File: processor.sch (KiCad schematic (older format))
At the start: 17 parts, among them U100 MC68000, U103 74F245, U104 74LS373, U105 74F245, U106 74LS373, U303 74F08

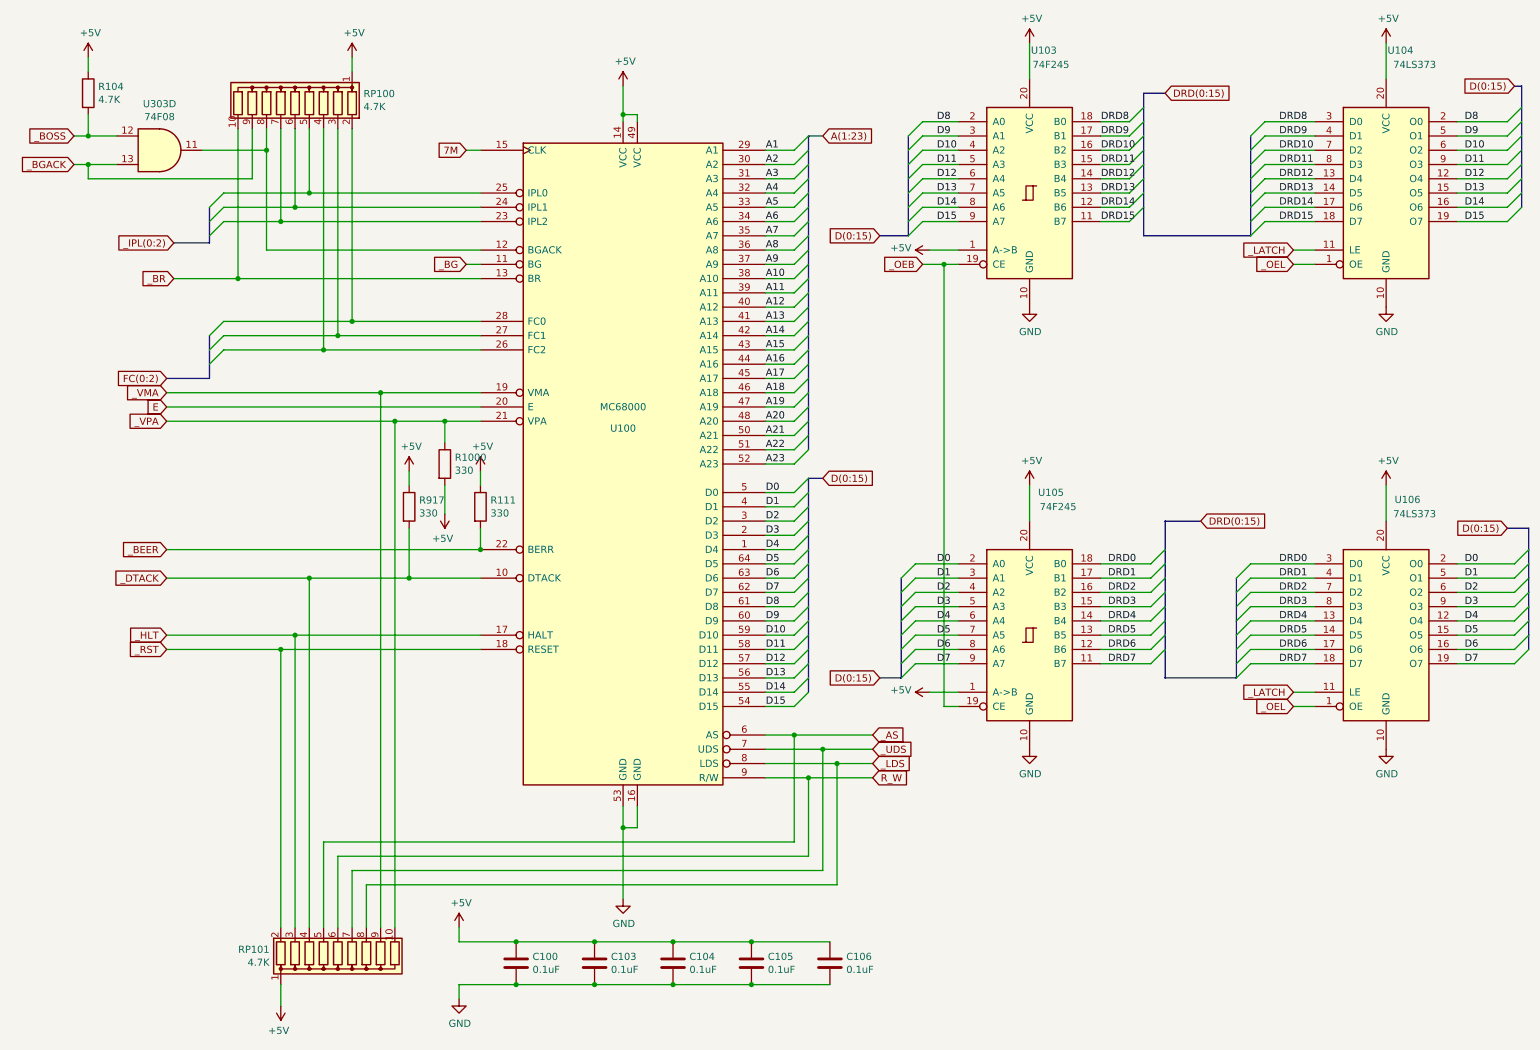
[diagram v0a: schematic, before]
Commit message: Rename bus with correct syntax
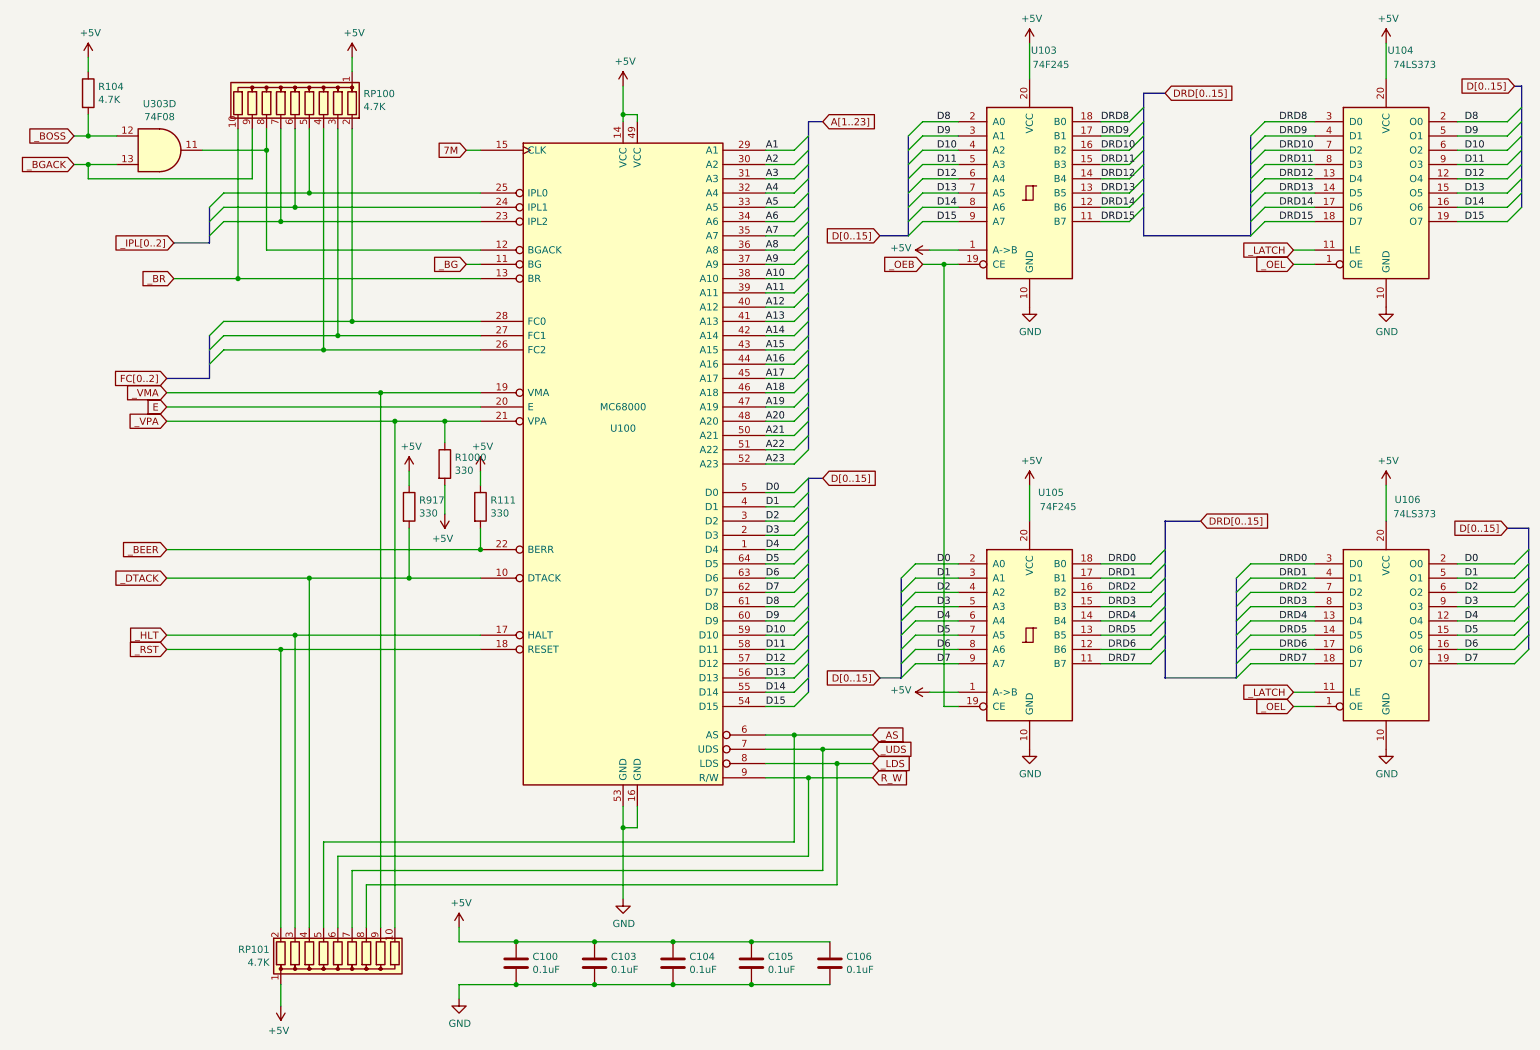
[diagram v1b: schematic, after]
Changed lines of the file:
@@
-EESchema Schematic File Version 4
+EESchema Schematic File Version 5
 LIBS:amiga2000-cache
 EELAYER 29 0
@@
 Wire Bus Line
 	6050 3850 6150 3850
-Wire Bus Line
-	6050 1450 6150 1450
-Text GLabel 6150 1450 2    50   Input ~ 0
-A(1:23)
+Text GLabel 6150 1350 2    50   Input ~ 0
+A[1..23]
 Text GLabel 6150 3850 2    50   Input ~ 0
-D(0:15)
+D[0..15]
 Wire Wire Line
 	3750 4350 1550 4350
@@
 	1850 2200 1600 2200
 Text GLabel 1600 2200 0    50   Input ~ 0
-_IPL(0:2)
+_IPL[0..2]
 Wire Wire Line
 	3750 2250 2250 2250
@@
 	1850 3050 1950 2950
 Text GLabel 1550 3150 0    50   Input ~ 0
-FC(0:2)
+FC[0..2]
 Wire Bus Line
 	1550 3150 1850 3150
@@
 	6550 5250 6700 5250
 Text GLabel 6550 2150 0    50   Input ~ 0
-D(0:15)
+D[0..15]
 Text GLabel 6550 5250 0    50   Input ~ 0
-D(0:15)
+D[0..15]
 Text GLabel 9450 2350 0    50   Input ~ 0
 _OEL
@@
 	8300 2050 8400 1950
 Text GLabel 8550 1150 2    50   Input ~ 0
-DRD(0:15)
+DRD[0..15]
 Text Label 8100 1350 0    50   ~ 0
 DRD8
@@
 	8450 5150 8550 5050
 Text GLabel 8800 4150 2    50   Input ~ 0
-DRD(0:15)
+DRD[0..15]
 Text Label 8150 4450 0    50   ~ 0
 DRD0
@@
 	8550 4150 8800 4150
 Text GLabel 11000 1100 0    50   Input ~ 0
-D(0:15)
+D[0..15]
 Text GLabel 10950 4200 0    50   Input ~ 0
-D(0:15)
+D[0..15]
 Text Label 10650 1350 0    50   ~ 0
 D8
@@
 	3500 3450 3150 3450
 Connection ~ 3750 4350
+Wire Bus Line
+	6050 1350 6150 1350
 $Comp
 L CPU_NXP_68000:68000D U100
@@
 	6050 3850 6050 5350
 Wire Bus Line
-	6050 1450 6050 3650
+	6050 1350 6050 3650
 $EndSCHEMATC

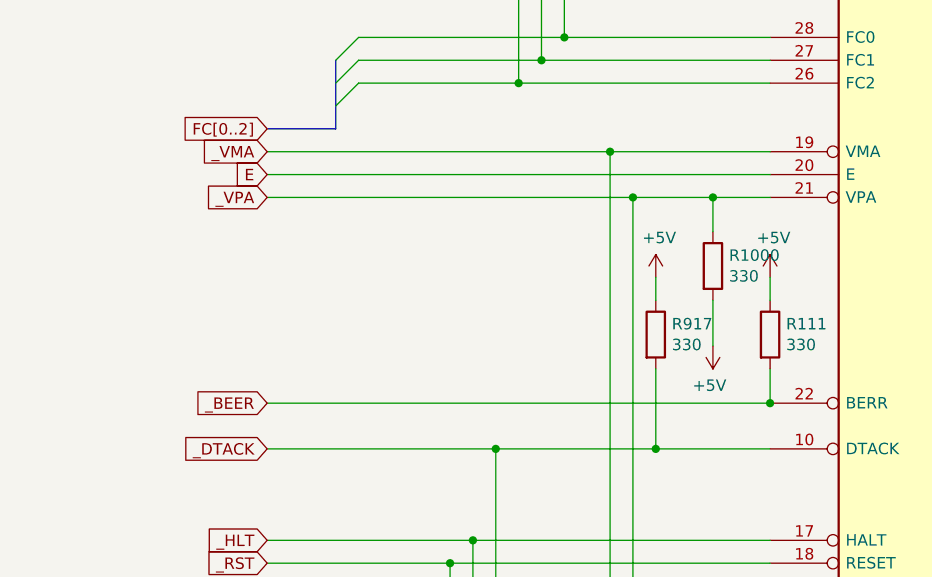
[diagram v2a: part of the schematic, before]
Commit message: Implemented various rev 6.2 fixes from forums and my own board
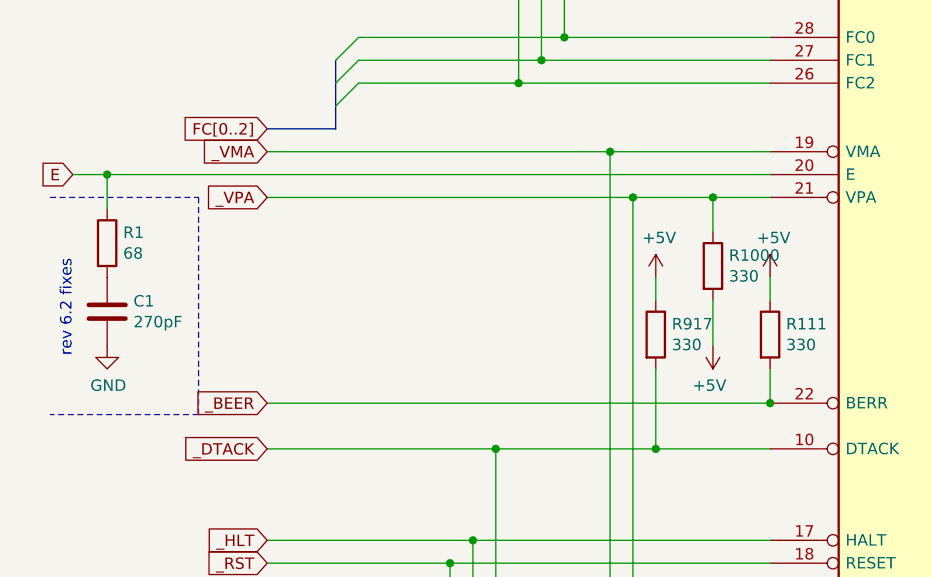
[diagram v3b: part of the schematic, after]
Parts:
- added C1: 270pF, symbol Device:C
- added R1: 68, symbol Device:R
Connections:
- net E: now also R1.1
- net GND: now also C1.2
- new net: C1.1, R1.2
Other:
- note added: "rev 6.2 fixes"
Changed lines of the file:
@@
 	3650 1550 3750 1550
 Wire Wire Line
-	1550 3350 3750 3350
-Text GLabel 1550 3350 0    50   Input ~ 0
+	700  3350 850  3350
+Text GLabel 700  3350 0    50   Input ~ 0
 E
 Wire Wire Line
@@
 	1    0    0    -1
 $EndComp
+$Comp
+L Device:R R1
+U 1 1 5D139FBE
+P 850 3650
+F 0 "R1" H 920 3696 50  0000 L CNN
+F 1 "68" H 920 3605 50  0000 L CNN
+F 2 "" V 780 3650 50  0001 C CNN
+F 3 "~" H 850 3650 50  0001 C CNN
+	1    850  3650
+	1    0    0    -1
+$EndComp
+$Comp
+L Device:C C1
+U 1 1 5D13AB75
+P 850 3950
+F 0 "C1" H 965 3996 50  0000 L CNN
+F 1 "270pF" H 965 3905 50  0000 L CNN
+F 2 "" H 888 3800 50  0001 C CNN
+F 3 "~" H 850 3950 50  0001 C CNN
+	1    850  3950
+	1    0    0    -1
+$EndComp
+$Comp
+L power:GND #PWR0262
+U 1 1 5D13B4A3
+P 850 4100
+F 0 "#PWR0262" H 850 3850 50  0001 C CNN
+F 1 "GND" H 855 3927 50  0000 C CNN
+F 2 "" H 850 4100 50  0001 C CNN
+F 3 "" H 850 4100 50  0001 C CNN
+	1    850  4100
+	1    0    0    -1
+$EndComp
+Wire Wire Line
+	850  3350 850  3500
+Connection ~ 850  3350
+Wire Wire Line
+	850  3350 3750 3350
+Wire Notes Line
+	600  3450 1250 3450
+Wire Notes Line
+	1250 3450 1250 4400
+Wire Notes Line
+	1250 4400 600  4400
 Wire Bus Line
 	1850 1950 1850 2200
@@
 Wire Bus Line
 	6050 1350 6050 3650
+Text Notes 700  4150 1    50   ~ 0
+rev 6.2 fixes
 $EndSCHEMATC

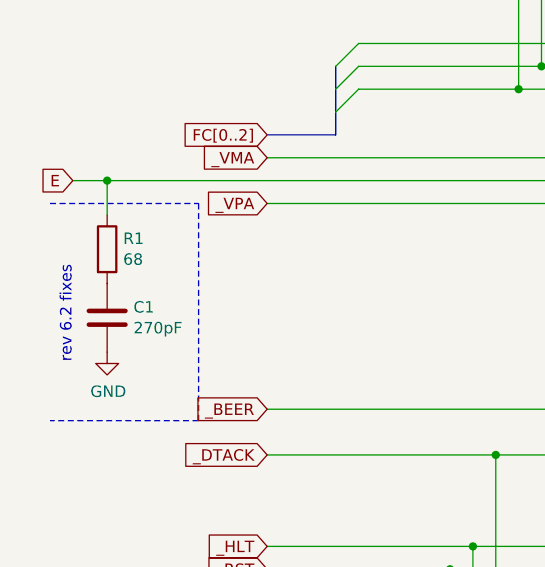
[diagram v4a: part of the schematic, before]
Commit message: Misread the PCB; It's effectively E and not A1
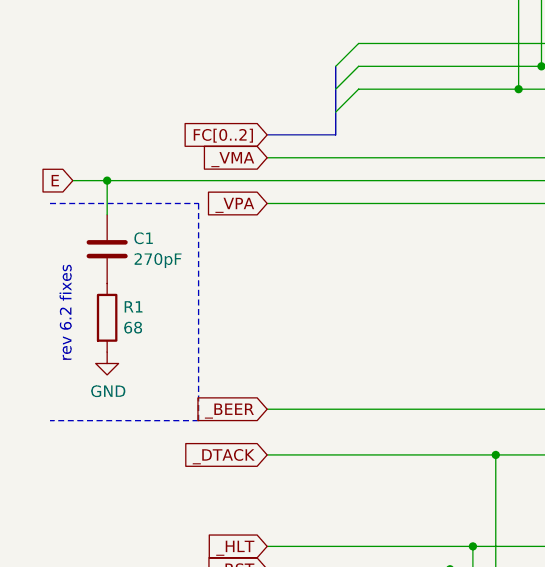
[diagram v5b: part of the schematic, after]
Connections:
- net E: now also C1.1; no longer R1.1
- net GND: now also R1.2; no longer C1.2
- new net: C1.2, R1.1
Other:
- moved on the sheet: C1, R1
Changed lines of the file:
@@
 L Device:R R1
 U 1 1 5D139FBE
-P 850 3650
-F 0 "R1" H 920 3696 50  0000 L CNN
-F 1 "68" H 920 3605 50  0000 L CNN
-F 2 "" V 780 3650 50  0001 C CNN
-F 3 "~" H 850 3650 50  0001 C CNN
-	1    850  3650
+P 850 3950
+F 0 "R1" H 920 3996 50  0000 L CNN
+F 1 "68" H 920 3905 50  0000 L CNN
+F 2 "" V 780 3950 50  0001 C CNN
+F 3 "~" H 850 3950 50  0001 C CNN
+	1    850  3950
 	1    0    0    -1
 $EndComp
@@
 L Device:C C1
 U 1 1 5D13AB75
-P 850 3950
-F 0 "C1" H 965 3996 50  0000 L CNN
-F 1 "270pF" H 965 3905 50  0000 L CNN
-F 2 "" H 888 3800 50  0001 C CNN
-F 3 "~" H 850 3950 50  0001 C CNN
-	1    850  3950
+P 850 3650
+F 0 "C1" H 965 3696 50  0000 L CNN
+F 1 "270pF" H 965 3605 50  0000 L CNN
+F 2 "" H 888 3500 50  0001 C CNN
+F 3 "~" H 850 3650 50  0001 C CNN
+	1    850  3650
 	1    0    0    -1
 $EndComp
@@
 Wire Notes Line
 	1250 4400 600  4400
+Text Notes 700  4150 1    50   ~ 0
+rev 6.2 fixes
 Wire Bus Line
 	1850 1950 1850 2200
@@
 Wire Bus Line
 	6050 1350 6050 3650
-Text Notes 700  4150 1    50   ~ 0
-rev 6.2 fixes
 $EndSCHEMATC

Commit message: Review started; oopsie whoopsie
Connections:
- net _IPL2: now reaches RP100.7 (R6), U100.23 (IPL2)
- net _IPL1: now reaches RP100.6 (R5), U100.24 (IPL1)
- net _IPL0: now reaches RP100.5 (R4), U100.25 (IPL0)
- net FC2: now reaches RP100.4 (R3), U100.26 (FC2)
- net FC1: now reaches RP100.3 (R2), U100.27 (FC1)
- net FC0: now reaches RP100.2 (R1), U100.28 (FC0)
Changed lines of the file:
@@
 Wire Bus Line
 	6050 1350 6050 3650
+Text Label 3500 1850 0    50   ~ 0
+_IPL0
+Text Label 3500 1950 0    50   ~ 0
+_IPL1
+Text Label 3500 2050 0    50   ~ 0
+_IPL2
+Text Label 3550 2750 0    50   ~ 0
+FC0
+Text Label 3550 2850 0    50   ~ 0
+FC1
+Text Label 3550 2950 0    50   ~ 0
+FC2
 $EndSCHEMATC

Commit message: Associate footprints with components
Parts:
- R1, R1000, R104, R111, R917: footprint (none) -> Resistor_THT:R_Axial_DIN0207_L6.3mm_D2.5mm_P10.16mm_Horizontal
- U103, U104, U105, U106: footprint (none) -> Package_DIP:DIP-20_W7.62mm_Socket
- U303: footprint (none) -> Package_DIP:DIP-14_W7.62mm_Socket
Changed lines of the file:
@@
 F 0 "U103" H 7700 2850 50  0000 C CNN
 F 1 "74F245" H 7750 2750 50  0000 C CNN
-F 2 "" H 7600 1850 50  0001 C CNN
+F 2 "Package_DIP:DIP-20_W7.62mm_Socket" H 7600 1850 50  0001 C CNN
 F 3 "http://www.ti.com/lit/gpn/sn74LS245" H 7600 1850 50  0001 C CNN
 	1    7600 1850
@@
 F 0 "U105" H 7750 5950 50  0000 C CNN
 F 1 "74F245" H 7800 5850 50  0000 C CNN
-F 2 "" H 7600 4950 50  0001 C CNN
+F 2 "Package_DIP:DIP-20_W7.62mm_Socket" H 7600 4950 50  0001 C CNN
 F 3 "http://www.ti.com/lit/gpn/sn74LS245" H 7600 4950 50  0001 C CNN
 	1    7600 4950
@@
 F 0 "U104" H 10200 2850 50  0000 C CNN
 F 1 "74LS373" H 10300 2750 50  0000 C CNN
-F 2 "" H 10100 1850 50  0001 C CNN
+F 2 "Package_DIP:DIP-20_W7.62mm_Socket" H 10100 1850 50  0001 C CNN
 F 3 "http://www.ti.com/lit/gpn/sn74LS373" H 10100 1850 50  0001 C CNN
 	1    10100 1850
@@
 F 0 "U106" H 10250 5900 50  0000 C CNN
 F 1 "74LS373" H 10300 5800 50  0000 C CNN
-F 2 "" H 10100 4950 50  0001 C CNN
+F 2 "Package_DIP:DIP-20_W7.62mm_Socket" H 10100 4950 50  0001 C CNN
 F 3 "http://www.ti.com/lit/gpn/sn74LS373" H 10100 4950 50  0001 C CNN
 	1    10100 4950
@@
 F 0 "U303" H 1500 1875 50  0000 C CNN
 F 1 "74F08" H 1500 1784 50  0000 C CNN
-F 2 "" H 1500 1550 50  0001 C CNN
+F 2 "Package_DIP:DIP-14_W7.62mm_Socket" H 1500 1550 50  0001 C CNN
 F 3 "http://www.ti.com/lit/gpn/sn74LS08" H 1500 1550 50  0001 C CNN
 	4    1500 1550
@@
 F 0 "R104" H 1070 1196 50  0000 L CNN
 F 1 "4.7K" H 1070 1105 50  0000 L CNN
-F 2 "" V 930 1150 50  0001 C CNN
+F 2 "Resistor_THT:R_Axial_DIN0207_L6.3mm_D2.5mm_P10.16mm_Horizontal" V 930 1150 50  0001 C CNN
 F 3 "~" H 1000 1150 50  0001 C CNN
 	1    1000 1150
@@
 F 0 "R111" H 3820 4096 50  0000 L CNN
 F 1 "330" H 3820 4005 50  0000 L CNN
-F 2 "" V 3680 4050 50  0001 C CNN
+F 2 "Resistor_THT:R_Axial_DIN0207_L6.3mm_D2.5mm_P10.16mm_Horizontal" V 3680 4050 50  0001 C CNN
 F 3 "~" H 3750 4050 50  0001 C CNN
 	1    3750 4050
@@
 F 0 "R917" H 3320 4096 50  0000 L CNN
 F 1 "330" H 3320 4005 50  0000 L CNN
-F 2 "" V 3180 4050 50  0001 C CNN
+F 2 "Resistor_THT:R_Axial_DIN0207_L6.3mm_D2.5mm_P10.16mm_Horizontal" V 3180 4050 50  0001 C CNN
 F 3 "~" H 3250 4050 50  0001 C CNN
 	1    3250 4050
@@
 F 0 "R1000" H 3570 3796 50  0000 L CNN
 F 1 "330" H 3570 3705 50  0000 L CNN
-F 2 "" V 3430 3750 50  0001 C CNN
+F 2 "Resistor_THT:R_Axial_DIN0207_L6.3mm_D2.5mm_P10.16mm_Horizontal" V 3430 3750 50  0001 C CNN
 F 3 "~" H 3500 3750 50  0001 C CNN
 	1    3500 3750
@@
 F 0 "R1" H 920 3996 50  0000 L CNN
 F 1 "68" H 920 3905 50  0000 L CNN
-F 2 "" V 780 3950 50  0001 C CNN
+F 2 "Resistor_THT:R_Axial_DIN0207_L6.3mm_D2.5mm_P10.16mm_Horizontal" V 780 3950 50  0001 C CNN
 F 3 "~" H 850 3950 50  0001 C CNN
 	1    850  3950
@@
 Wire Bus Line
 	6050 3850 6150 3850
-Wire Bus Line
-	1850 1950 1850 2200
-Wire Bus Line
-	1850 2850 1850 3150
-Wire Bus Line
-	6750 1450 6750 2150
-Wire Bus Line
-	6700 4550 6700 5250
-Wire Bus Line
-	9150 1450 9150 2150
-Wire Bus Line
-	9050 4550 9050 5250
-Wire Bus Line
-	11050 1100 11050 1950
-Wire Bus Line
-	11100 4200 11100 5050
-Wire Bus Line
-	8550 4150 8550 5250
-Wire Bus Line
-	8400 1150 8400 2150
-Wire Bus Line
-	6050 3850 6050 5350
-Wire Bus Line
-	6050 1350 6050 3650
 Text Label 3500 1850 0    50   ~ 0
 _IPL0
@@
 Text Label 3550 2950 0    50   ~ 0
 FC2
+Wire Bus Line
+	1850 1950 1850 2200
+Wire Bus Line
+	1850 2850 1850 3150
+Wire Bus Line
+	6750 1450 6750 2150
+Wire Bus Line
+	6700 4550 6700 5250
+Wire Bus Line
+	9150 1450 9150 2150
+Wire Bus Line
+	9050 4550 9050 5250
+Wire Bus Line
+	11050 1100 11050 1950
+Wire Bus Line
+	11100 4200 11100 5050
+Wire Bus Line
+	8550 4150 8550 5250
+Wire Bus Line
+	8400 1150 8400 2150
+Wire Bus Line
+	6050 3850 6050 5350
+Wire Bus Line
+	6050 1350 6050 3650
 $EndSCHEMATC
